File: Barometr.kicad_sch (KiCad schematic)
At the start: 4 parts, among them U600 TJA1044GTK_3Z

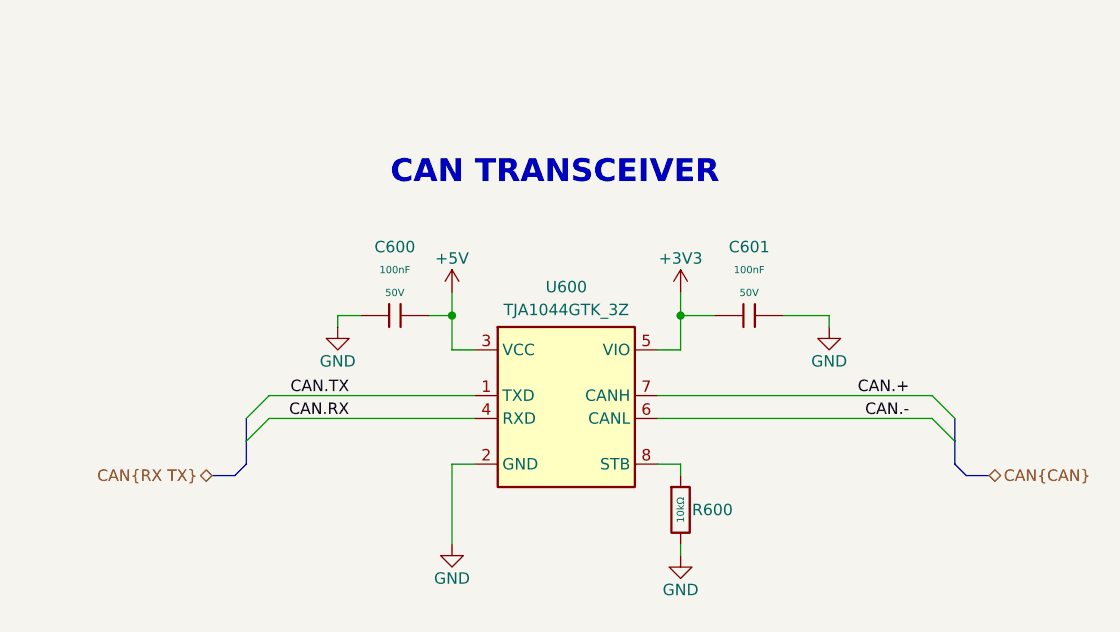
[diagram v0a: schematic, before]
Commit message: [barometer] added presure sensor
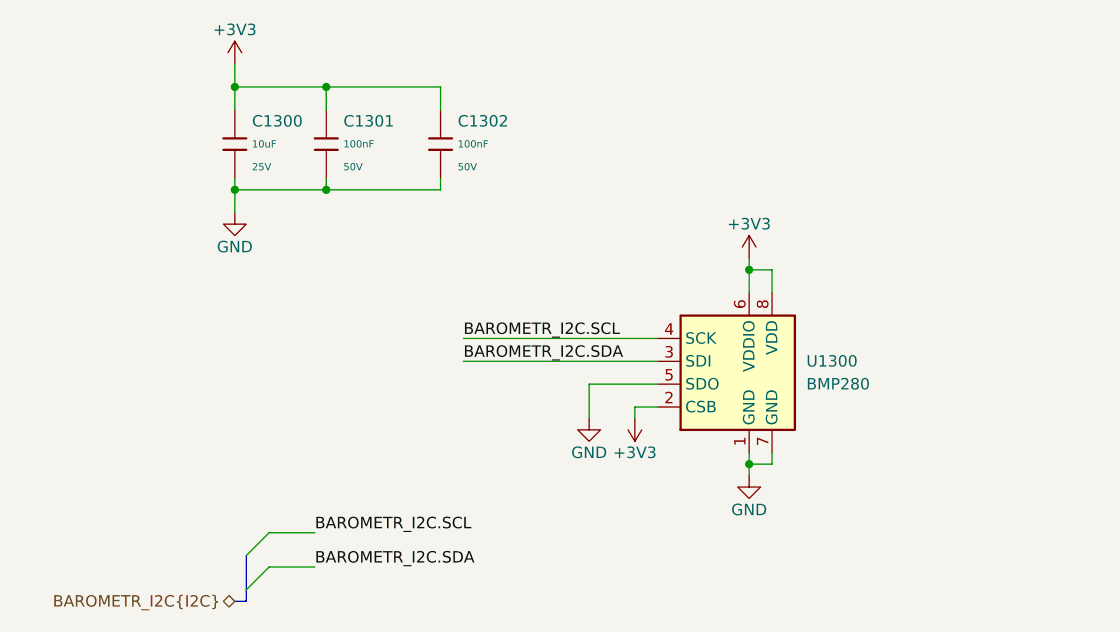
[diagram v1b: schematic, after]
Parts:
- removed C600, C601: 100nF, PCM_JLCPCB:C_0402, symbol PCM_JLCPCB-Capacitors:0402,100nF,(2)
- removed R600: 10kΩ, PCM_JLCPCB:R_0402, symbol PCM_JLCPCB-Resistors:0402,10kΩ
- removed U600: TJA1044GTK_3Z, Package_SON:HVSON-8-1EP_3x3mm_P0.65mm_EP1.6x2.4mm, symbol TJA1044GTK_3Z:TJA1044GTK_3Z
- added C1300: 10uF, PCM_JLCPCB:C_0603, symbol PCM_JLCPCB-Capacitors:0603,10uF,(2)
- added C1301, C1302: 100nF, PCM_JLCPCB:C_0402, symbol PCM_JLCPCB-Capacitors:0402,100nF,(2)
- added U1300: BMP280, Package_LGA:Bosch_LGA-8_2x2.5mm_P0.65mm_ClockwisePinNumbering, symbol Sensor_Pressure:BMP280
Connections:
- net +3V3: now also C1300.1, C1301.1, C1302.1, U1300.2 (CSB), U1300.6 (VDDIO), U1300.8 (VDD)
- net GND: now also C1300.2, C1301.2, C1302.2, U1300.1 (GND), U1300.5 (SDO), U1300.7 (GND)
- new net BAROMETR_I2C.SCL: U1300.4 (SCK)
- new net BAROMETR_I2C.SDA: U1300.3 (SDI)
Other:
- note removed: "CAN TRANSCEIVER"
- company: KoNaR -> (none)
- title: ModuCard nav module -> (none)
